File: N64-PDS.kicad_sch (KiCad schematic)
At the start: 38 parts, among them J1 PWR_OUT, J2 I2C_OUT, J3 USB-C-6P-PWR, U1 ST1S41PHR, U2 ST1S41PHR, U3 STL6P3LLH6, U4 STUSB4500QTR

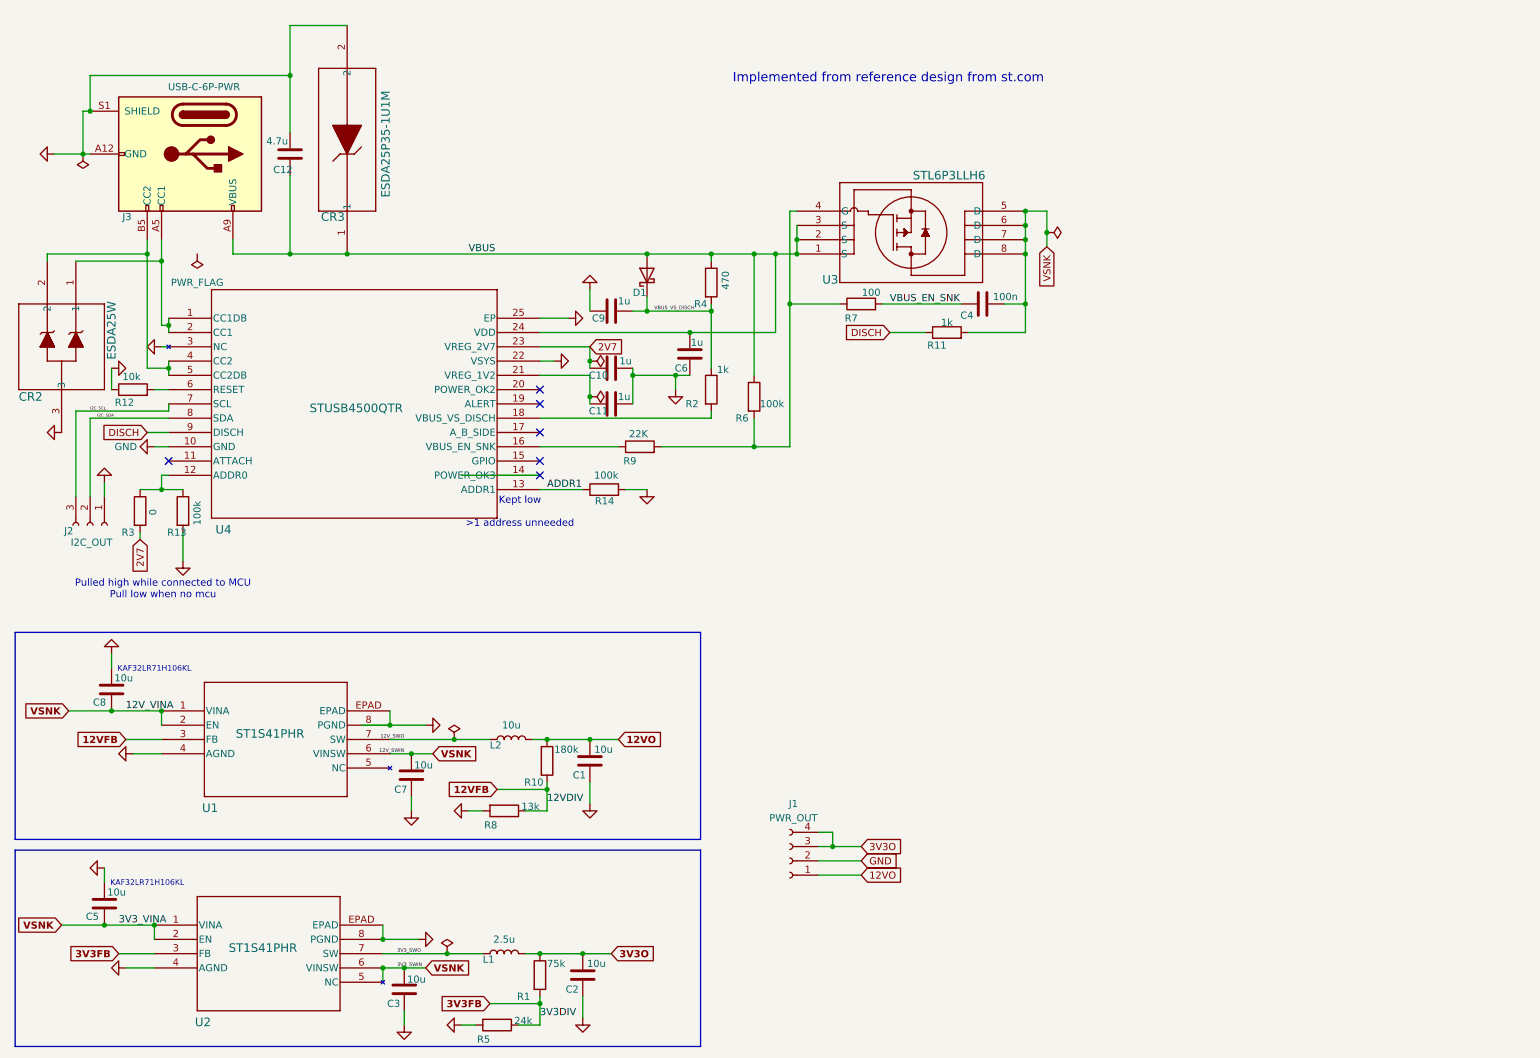
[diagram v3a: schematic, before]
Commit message: Component switch
Switch buck/boost converter components, Complete schematic
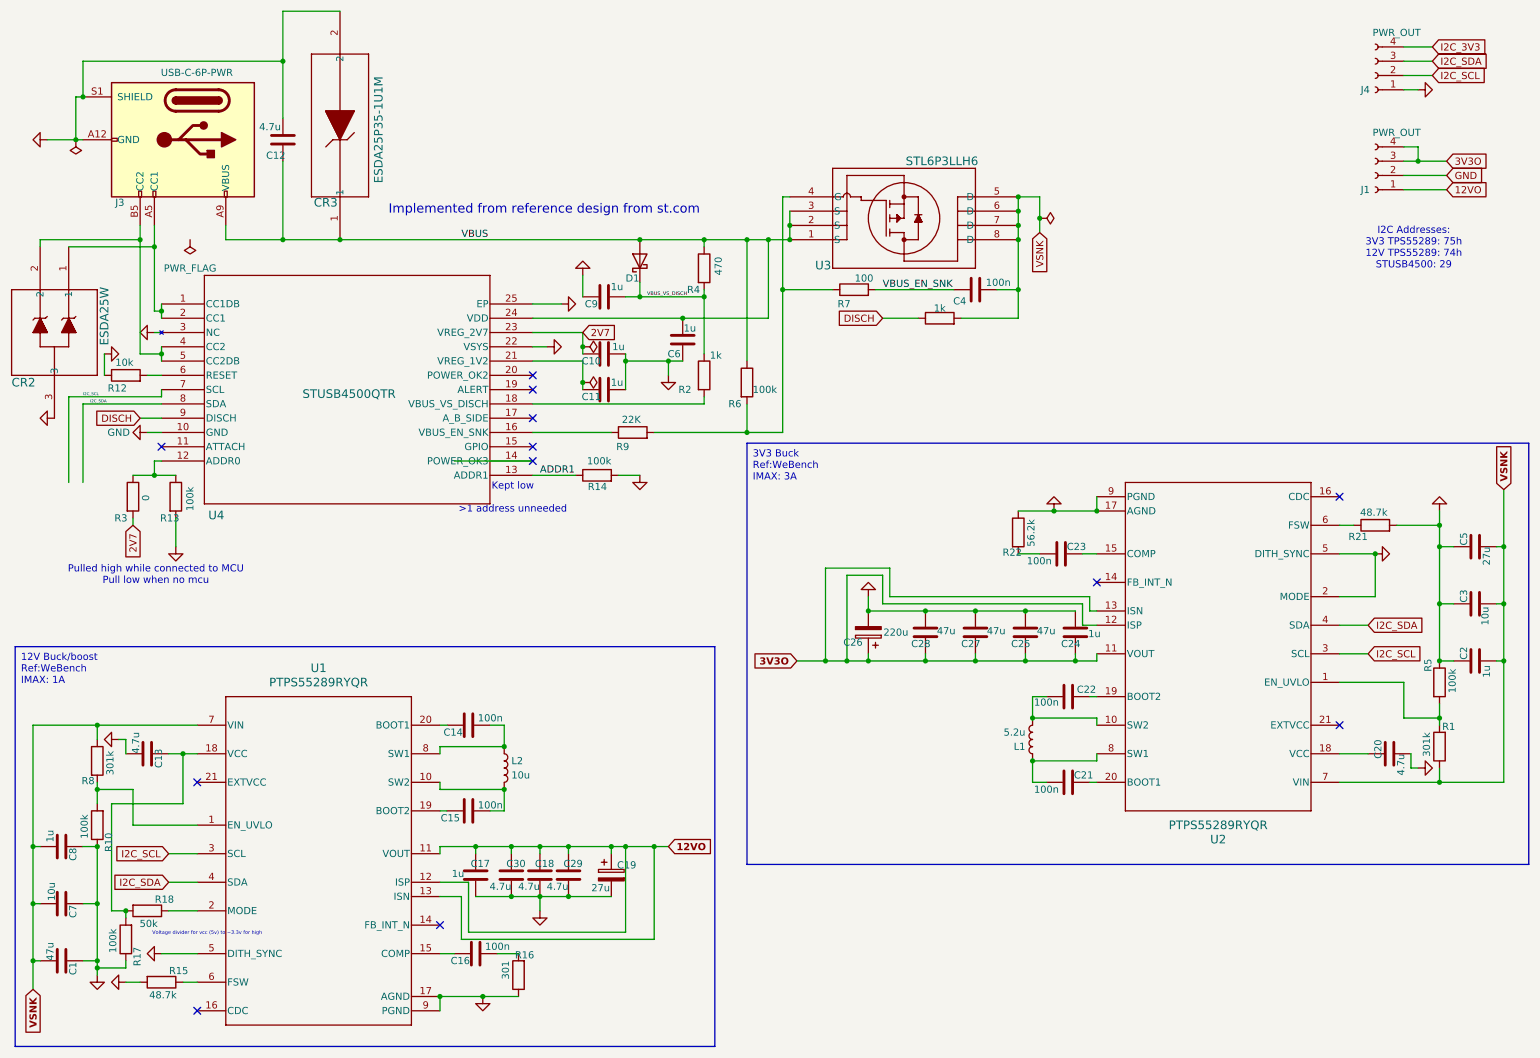
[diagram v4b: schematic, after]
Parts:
- removed J2: I2C_OUT, Connector_Wire:SolderWire-1.5sqmm_1x03_P6mm_D1.7mm_OD3mm, symbol Connector:Conn_01x03_Socket
- removed U1, U2: ST1S41PHR, ST1S41PHR:HSOP8_STM-M, symbol ST1S41PHR:ST1S41PHR
- added C13, C18, C20, C29, C30: 4.7u, symbol Device:C
- added C14, C15, C16, C21, C22, C23: 100n, symbol Device:C
- added C17, C24: 1u, symbol Device:C
- added C19: 27u, symbol Device:C_Polarized
- added C25, C27, C28: 47u, symbol Device:C
- added C26: 220u, symbol Device:C_Polarized
- added J4: PWR_OUT, Connector_JST:JST_NV_B04P-NV_1x04_P5.00mm_Vertical, symbol Connector:Conn_01x04_Socket
- added R15, R21: 48.7k, Resistor_SMD:R_0402_1005Metric_Pad0.72x0.64mm_HandSolder, symbol Device:R
- added R16: 301, Resistor_SMD:R_0402_1005Metric_Pad0.72x0.64mm_HandSolder, symbol Device:R
- added R17: 100k, Resistor_SMD:R_0402_1005Metric_Pad0.72x0.64mm_HandSolder, symbol Device:R
- added R18: 50k, Resistor_SMD:R_0402_1005Metric_Pad0.72x0.64mm_HandSolder, symbol Device:R
- added R22: 56.2k, Resistor_SMD:R_0402_1005Metric_Pad0.72x0.64mm_HandSolder, symbol Device:R
- added U1, U2: PTPS55289RYQR, RYQ0021A-MFG, symbol PTPS55289RYQR:PTPS55289RYQR
- C1: value 10u -> 47u; footprint Capacitor_SMD:C_0805_2012Metric_Pad1.18x1.45mm_HandSolder -> (none)
- C2: value 10u -> 1u; footprint Capacitor_SMD:C_0805_2012Metric_Pad1.18x1.45mm_HandSolder -> (none)
- C3: footprint Capacitor_SMD:C_0603_1608Metric -> (none)
- C5: value 10u -> 27u; footprint Capacitor_SMD:C_0603_1608Metric_Pad1.08x0.95mm_HandSolder -> (none)
- C7: footprint Capacitor_SMD:C_0805_2012Metric_Pad1.18x1.45mm_HandSolder -> (none)
- C8: value 10u -> 1u; footprint Capacitor_SMD:C_0603_1608Metric_Pad1.08x0.95mm_HandSolder -> (none)
- L1: value 2.5u -> 5.2u; footprint Inductor_SMD:L_Coilcraft_MSS1048-XXX -> Inductor_SMD:L_Coilcraft_XAL6060-XXX
- L2: footprint Inductor_SMD:L_Coilcraft_MSS1260-XXX -> (none)
- R1: value 75k -> 301k
- R10: value 180k -> 100k
- R5: value 24k -> 100k
- R8: value 13k -> 301k
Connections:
- net 12VO: now also C17.2, C18.2, C19.1, C29.2, C30.2, U1.11 (VOUT), U1.12 (ISP), U1.13 (ISN); no longer C1.1, L2.2, R10.1
- net 3V3O: now also C24.2, C25.2, C26.1, C27.2, C28.2, U2.11 (VOUT), U2.12 (ISP), U2.13 (ISN); no longer C2.1, L1.2, R1.1
- net GND: now also C5.2, C8.2, R10.1, R5.1, C13.1, C17.1, C18.1, C19.2, C20.1, C24.1, C25.1, C26.2, C27.1, C28.1, C29.1, C30.1, J4.1 (Pin_1), R15.2, R16.1, R17.1, R21.2, R22.1, U1.17 (AGND), U1.5 (DITH_SYNC), U1.9 (PGND), U2.17 (AGND), U2.2 (MODE), U2.5 (DITH_SYNC), U2.9 (PGND); no longer C5.1, C8.1, R5.2, R8.2
- net I2C_SCL: now also J4.2 (Pin_2), U1.3 (SCL), U2.3 (SCL)
- net I2C_SDA: now also J4.3 (Pin_3), U1.4 (SDA), U2.4 (SDA)
- net VSNK: now also C1.1, C2.1, C5.1, C8.1, R1.1, R8.1, U1.7 (VIN), U2.7 (VIN); no longer C5.2, C8.2
- net 12VFB: no longer names the net of R10.2
- net 12VFB: now also R8.2, U1.1 (EN_UVLO); no longer R8.1
- net 12V_SWO: no longer names the net of L2.1
- net 12V_SWO: now also C14.2, U1.8 (SW1)
- net 3V3FB: no longer names the net of R1.2
- net 3V3FB: now also R5.2, U2.1 (EN_UVLO); no longer R5.1
- net 3V3_SWO: no longer names the net of L1.1
- net 3V3_SWO: now also C21.2, U2.8 (SW1)
- new net: C21.1, U2.20 (BOOT1)
- new net: C22.2, L1.2, U2.10 (SW2)
- new net: C14.1, U1.20 (BOOT1)
- new net: C23.1, U2.15 (COMP)
- new net: C23.2, R22.2
- new net: C13.2, R17.2, R18.2, U1.18 (VCC)
- new net: C20.2, U2.18 (VCC)
- new net: R21.1, U2.6 (FSW)
- new net: C15.1, U1.19 (BOOT2)
- new net: C15.2, L2.2, U1.10 (SW2)
- new net: C16.1, U1.15 (COMP)
- new net: R18.1, U1.2 (MODE)
- new net: R15.1, U1.6 (FSW)
- new net: C16.2, R16.2
- new net: C22.1, U2.19 (BOOT2)
- new net I2C_3V3: J4.4 (Pin_4)
- no-connect marks 6 -> 12
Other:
- note added: "I2C Addresses: 3V3 TPS55289: 75h 12V TPS55289: 74h STUSB4500: 29"
- note added: "Voltage divider for vcc (5v) to ~3.3v for high"
- note removed: "KAF32LR71H106KL"
- moved on the sheet: C10, C11, C12, C4, C6, C9, CR2, CR3, D1, J1, J3, R12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

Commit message: Add footprint, assign all component footprints.
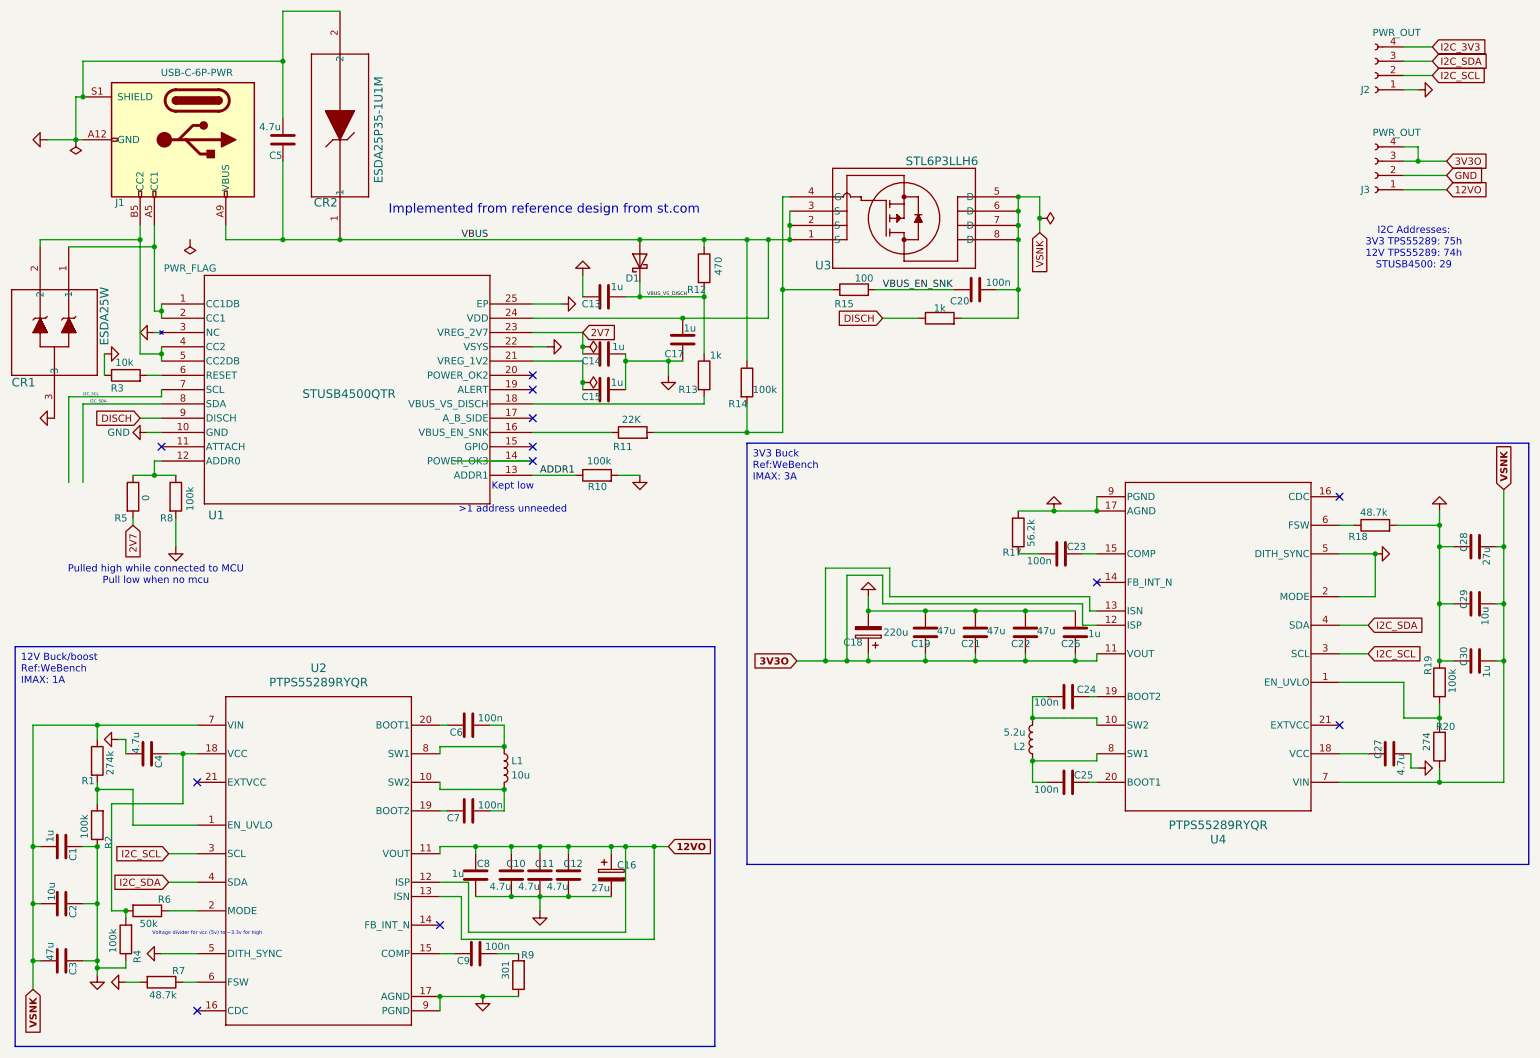
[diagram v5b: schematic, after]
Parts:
- C1: renamed from C8; footprint (none) -> Capacitor_SMD:C_0402_1005Metric_Pad0.74x0.62mm_HandSolder
- C10: renamed from C30; footprint (none) -> Capacitor_SMD:C_0805_2012Metric_Pad1.18x1.45mm_HandSolder
- C11: renamed from C18; footprint (none) -> Capacitor_SMD:C_0805_2012Metric_Pad1.18x1.45mm_HandSolder
- C12: renamed from C29; footprint (none) -> Capacitor_SMD:C_0805_2012Metric_Pad1.18x1.45mm_HandSolder
- C16: renamed from C19; footprint (none) -> Capacitor_SMD:CP_Elec_5x5.9
- C18: renamed from C26; footprint (none) -> Capacitor_SMD:CP_Elec_6.3x5.9
- C19: renamed from C28; footprint (none) -> Capacitor_SMD:C_0805_2012Metric_Pad1.18x1.45mm_HandSolder
- C2: renamed from C7; footprint (none) -> Capacitor_SMD:C_1210_3225Metric_Pad1.33x2.70mm_HandSolder
- C20: renamed from C4; footprint Capacitor_SMD:C_0504_1310Metric -> Capacitor_SMD:C_0504_1310Metric_Pad0.83x1.28mm_HandSolder
- C21: renamed from C27; footprint (none) -> Capacitor_SMD:C_0805_2012Metric_Pad1.18x1.45mm_HandSolder
- C22: renamed from C25; footprint (none) -> Capacitor_SMD:C_0805_2012Metric_Pad1.18x1.45mm_HandSolder
- C23: footprint (none) -> Capacitor_SMD:C_0402_1005Metric_Pad0.74x0.62mm_HandSolder
- C24: renamed from C22; footprint (none) -> Capacitor_SMD:C_0603_1608Metric_Pad1.08x0.95mm_HandSolder
- C25: renamed from C21; footprint (none) -> Capacitor_SMD:C_0603_1608Metric_Pad1.08x0.95mm_HandSolder
- C26: renamed from C24; footprint (none) -> Capacitor_SMD:C_0603_1608Metric_Pad1.08x0.95mm_HandSolder
- C27: renamed from C20; footprint (none) -> Capacitor_SMD:C_0603_1608Metric_Pad1.08x0.95mm_HandSolder
- C28: renamed from C5; footprint (none) -> Capacitor_SMD:C_Elec_5x5.8
- C29: renamed from C3; footprint (none) -> Capacitor_SMD:C_1210_3225Metric_Pad1.33x2.70mm_HandSolder
- C3: renamed from C1; footprint (none) -> Capacitor_SMD:C_Elec_6.3x5.8
- C30: renamed from C2; footprint (none) -> Capacitor_SMD:C_0402_1005Metric_Pad0.74x0.62mm_HandSolder
- C4: renamed from C13; footprint (none) -> Capacitor_SMD:C_0603_1608Metric_Pad1.08x0.95mm_HandSolder
- C6: renamed from C14; footprint (none) -> Capacitor_SMD:C_0603_1608Metric_Pad1.08x0.95mm_HandSolder
- C7: renamed from C15; footprint (none) -> Capacitor_SMD:C_0603_1608Metric_Pad1.08x0.95mm_HandSolder
- C8: renamed from C17; footprint (none) -> Capacitor_SMD:C_0603_1608Metric_Pad1.08x0.95mm_HandSolder
- C9: renamed from C16; footprint (none) -> Capacitor_SMD:C_0402_1005Metric_Pad0.74x0.62mm_HandSolder
- L1: renamed from L2; footprint (none) -> Library:DR1040-5R2-R
- R1: renamed from R8; value 301k -> 274k
- R20: renamed from R1; value 301k -> 274
- renumbered C9 to C13, C10 to C14, C11 to C15, C6 to C17, C12 to C5, CR2 to CR1, CR3 to CR2, J3 to J1, J4 to J2, J1 to J3, L1 to L2, R14 to R10, R9 to R11, R4 to R12, R2 to R13, R6 to R14, R7 to R15, R11 to R16, R22 to R17, R21 to R18, R5 to R19, R10 to R2, R12 to R3, R17 to R4, R3 to R5, R18 to R6, R15 to R7, R13 to R8, R16 to R9, U4 to U1, U1 to U2, U2 to U4

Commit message: Update board
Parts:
- J2: value PWR_OUT -> I2C_OUT; footprint Connector_JST:JST_NV_B04P-NV_1x04_P5.00mm_Vertical -> Connector_Molex:Molex_PicoBlade_53047-0410_1x04_P1.25mm_Vertical
- U2, U4: footprint RYQ0021A-MFG -> PTPS55289RYQR:RYQ0021A-MFG
- U3: footprint STL6P3LLH6:POWERFLAT_3P3X3P3_STM-M -> POWERFLAT_3P3X3P3_STM
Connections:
- net VSNK: now also U3.9
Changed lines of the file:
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@@
 	)
 	(junction
-		(at 40.64 73.66)
-		(diameter 0)
-		(color 0 0 0 0)
-	)
-	(junction
 		(at 25.4 35.56)
 		(diameter 0)
@@
 	)
 	(junction
+		(at 40.64 73.66)
+		(diameter 0)
+		(color 0 0 0 0)
+	)
+	(junction
 		(at 113.03 161.29)
 		(diameter 0)
@@
 	(wire
 		(pts
-			(xy 40.64 72.39) (xy 40.64 73.66)
-		)
-		(stroke
-			(width 0)
-			(type default)
-		)
-	)
-	(wire
-		(pts
 			(xy 115.57 72.39) (xy 115.57 73.66)
 		)
@@
 	(wire
 		(pts
+			(xy 40.64 72.39) (xy 40.64 73.66)
+		)
+		(stroke
+			(width 0)
+			(type default)
+		)
+	)
+	(wire
+		(pts
 			(xy 279.4 118.11) (xy 279.4 128.27)
 		)
@@
 	(wire
 		(pts
+			(xy 187.96 43.18) (xy 193.04 43.18)
+		)
+		(stroke
+			(width 0)
+			(type default)
+		)
+	)
+	(wire
+		(pts
 			(xy 34.29 172.72) (xy 31.75 172.72)
 		)
@@
 	(wire
 		(pts
+			(xy 193.04 43.18) (xy 193.04 45.72)
+		)
+		(stroke
+			(width 0)
+			(type default)
+		)
+	)
+	(wire
+		(pts
 			(xy 267.97 138.43) (xy 267.97 135.89)
 		)
@@
 	(wire
 		(pts
-			(xy 39.37 69.85) (xy 40.64 69.85)
-		)
-		(stroke
-			(width 0)
-			(type default)
-		)
-	)
-	(wire
-		(pts
 			(xy 20.32 35.56) (xy 25.4 35.56)
 		)
@@
 	(wire
 		(pts
+			(xy 40.64 69.85) (xy 39.37 69.85)
+		)
+		(stroke
+			(width 0)
+			(type default)
+		)
+	)
+	(wire
+		(pts
 			(xy 46.99 162.56) (xy 41.91 162.56)
 		)
@@
 		(lib_id "Device:R")
 		(at 144.78 78.74 0)
+		(mirror y)
 		(unit 1)
 		(exclude_from_sim no)
@@
 		(dnp no)
 		(property "Reference" "R14"
-			(at 141.478 82.55 0)
+			(at 148.082 82.55 0)
 			(effects
 				(font
@@
 		)
 		(property "Value" "100k"
-			(at 145.796 80.01 0)
+			(at 143.764 80.01 0)
 			(effects
 				(font
@@
 		)
 		(property "Footprint" "Resistor_SMD:R_0402_1005Metric_Pad0.72x0.64mm_HandSolder"
-			(at 143.002 78.74 90)
+			(at 146.558 78.74 90)
 			(effects
 				(font
@@
 			)
 		)
-		(property "Footprint" "RYQ0021A-MFG"
+		(property "Footprint" "PTPS55289RYQR:RYQ0021A-MFG"
 			(at 46.99 139.7 0)
 			(effects
@@
 	(symbol
 		(lib_id "power:GND")
-		(at 39.37 69.85 270)
-		(unit 1)
-		(exclude_from_sim no)
-		(in_bom yes)
-		(on_board yes)
-		(dnp no)
-		(property "Reference" "#PWR08"
-			(at 33.02 69.85 0)
-			(effects
-				(font
-					(size 1.27 1.27)
-				)
-				(hide yes)
-			)
-		)
-		(property "Value" "GND"
-			(at 34.29 69.85 90)
-			(effects
-				(font
-					(size 1.27 1.27)
-				)
-				(hide yes)
-			)
-		)
-		(property "Footprint" ""
-			(at 39.37 69.85 0)
-			(effects
-				(font
-					(size 1.27 1.27)
-				)
-				(hide yes)
-			)
-		)
-		(property "Datasheet" ""
-			(at 39.37 69.85 0)
-			(effects
-				(font
-					(size 1.27 1.27)
-				)
-				(hide yes)
-			)
-		)
-		(property "Description" "Power symbol creates a global label with name \"GND\" , ground"
-			(at 39.37 69.85 0)
-			(effects
-				(font
-					(size 1.27 1.27)
-				)
-				(hide yes)
-			)
-		)
-		(pin "1"
-		)
-		(instances
-			(project "N64-PDS"
-				(path "/9649f91c-0b3c-463e-88a6-37fb387993ef"
-					(reference "#PWR08")
-					(unit 1)
-				)
-			)
-		)
-	)
-	(symbol
-		(lib_id "power:GND")
 		(at 111.76 64.77 90)
 		(unit 1)
@@
 			)
 		)
-		(property "Footprint" "STL6P3LLH6:POWERFLAT_3P3X3P3_STM-M"
+		(property "Footprint" "POWERFLAT_3P3X3P3_STM"
 			(at 152.4 53.34 0)
 			(effects
@@
 		(pin "3"
 		)
+		(pin "9"
+		)
 		(instances
 			(project ""
@@
 	(symbol
 		(lib_id "power:GND")
+		(at 39.37 69.85 0)
+		(unit 1)
+		(exclude_from_sim no)
+		(in_bom yes)
+		(on_board yes)
+		(dnp no)
+		(property "Reference" "#PWR08"
+			(at 39.37 76.2 0)
+			(effects
+				(font
+					(size 1.27 1.27)
+				)
+				(hide yes)
+			)
+		)
+		(property "Value" "GND"
+			(at 39.37 74.93 90)
+			(effects
+				(font
+					(size 1.27 1.27)
+				)
+				(hide yes)
+			)
+		)
+		(property "Footprint" ""
+			(at 39.37 69.85 0)
+			(effects
+				(font
+					(size 1.27 1.27)
+				)
+				(hide yes)
+			)
+		)
+		(property "Datasheet" ""
+			(at 39.37 69.85 0)
+			(effects
+				(font
+					(size 1.27 1.27)
+				)
+				(hide yes)
+			)
+		)
+		(property "Description" "Power symbol creates a global label with name \"GND\" , ground"
+			(at 39.37 69.85 0)
+			(effects
+				(font
+					(size 1.27 1.27)
+				)
+				(hide yes)
+			)
+		)
+		(pin "1"
+		)
+		(instances
+			(project "N64-PDS"
+				(path "/9649f91c-0b3c-463e-88a6-37fb387993ef"
+					(reference "#PWR08")
+					(unit 1)
+				)
+			)
+		)
+	)
+	(symbol
+		(lib_id "power:GND")
 		(at 115.57 59.69 180)
 		(unit 1)
@@
 			)
 		)
-		(property "Footprint" "RYQ0021A-MFG"
+		(property "Footprint" "PTPS55289RYQR:RYQ0021A-MFG"
 			(at 250.19 149.86 0)
 			(effects
@@
 			)
 		)
-		(property "Value" "PWR_OUT"
+		(property "Value" "I2C_OUT"
 			(at 260.35 16.51 0)
 			(effects
@@
 			)
 		)
-		(property "Footprint" "Connector_JST:JST_NV_B04P-NV_1x04_P5.00mm_Vertical"
+		(property "Footprint" "Connector_Molex:Molex_PicoBlade_53047-0410_1x04_P1.25mm_Vertical"
 			(at 256.54 24.13 0)
 			(effects
